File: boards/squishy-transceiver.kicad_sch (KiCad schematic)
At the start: 99 parts, among them Q2 Q_PMOS_DGS, Q3 Q_DUAL_PMOS_S1G1D2S2G2D1, Q4 Q_DUAL_PMOS_S1G1D2S2G2D1, U10 FXL4TD245BQX, U11 FXL4TD245BQX, U12 FXL4TD245BQX, U13 FXL4TD245BQX, U14 FXL4TD245BQX, U15 FXL4TD245BQX, U16 FXL4TD245BQX, U17 THVD1452DGSR, U18 THVD1452DGSR, U19 THVD1452DGSR, U20 THVD1452DGSR, U21 THVD1452DGSR, U22 THVD1452DGSR, U23 THVD1452DGSR, U24 THVD1452DGSR, U25 THVD1452DGSR, U26 THVD1452DGSR, U27 THVD1452DGSR, U28 THVD1452DGSR, U29 THVD1452DGSR, U30 THVD1452DGSR, U31 THVD1452DGSR, U32 THVD1452DGSR, U33 THVD1452DGSR, U34 THVD1452DGSR, U8 FXL4TD245BQX, U9 FXL4TD245BQX

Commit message: hardware: a bunch of clean up and the like
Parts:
- renumbered R51 to R11, R27 to R12, R24 to R15, R57 to R18, R39 to R22, R18 to R23, R48 to R24, R15 to R25, R12 to R26, R45 to R27, R9 to R28, R60 to R29, R33 to R3, R75 to R30, R8 to R31, R76 to R32, R10 to R33, R44 to R34, R78 to R35, R46 to R36, R83 to R37, R73 to R38, R11 to R39, R54 to R4, R77 to R40, R13 to R41, R14 to R42, R16 to R43, R61 to R44, R47 to R45, R84 to R46, R49 to R47, R17 to R48, R19 to R49, R36 to R5, R38 to R50, R40 to R51, R20 to R54, R22 to R55, R23 to R59, R25 to R60, R26 to R61, R28 to R63, R50 to R64, R80 to R65, R52 to R66, R81 to R67, R72 to R68, R29 to R69, R79 to R70, R31 to R71, R62 to R73, R41 to R74, R82 to R75, R43 to R76, R5 to R78, R7 to R79, R42 to R8, R35 to R80, R37 to R81, R53 to R82, R55 to R83, R32 to R84, R34 to R85, R30 to R9, U26 to U1, U29 to U10, U10 to U11, U25 to U13, U32 to U15, U11 to U16, U24 to U17, U23 to U18, U8 to U2, U12 to U20, U34 to U21, U13 to U23, U28 to U24, U21 to U25, U14 to U27, U31 to U28, U20 to U29, U15 to U30, U19 to U31, U30 to U32, U16 to U33, U18 to U34, U33 to U4, U27 to U6, U9 to U8, U17 to U9

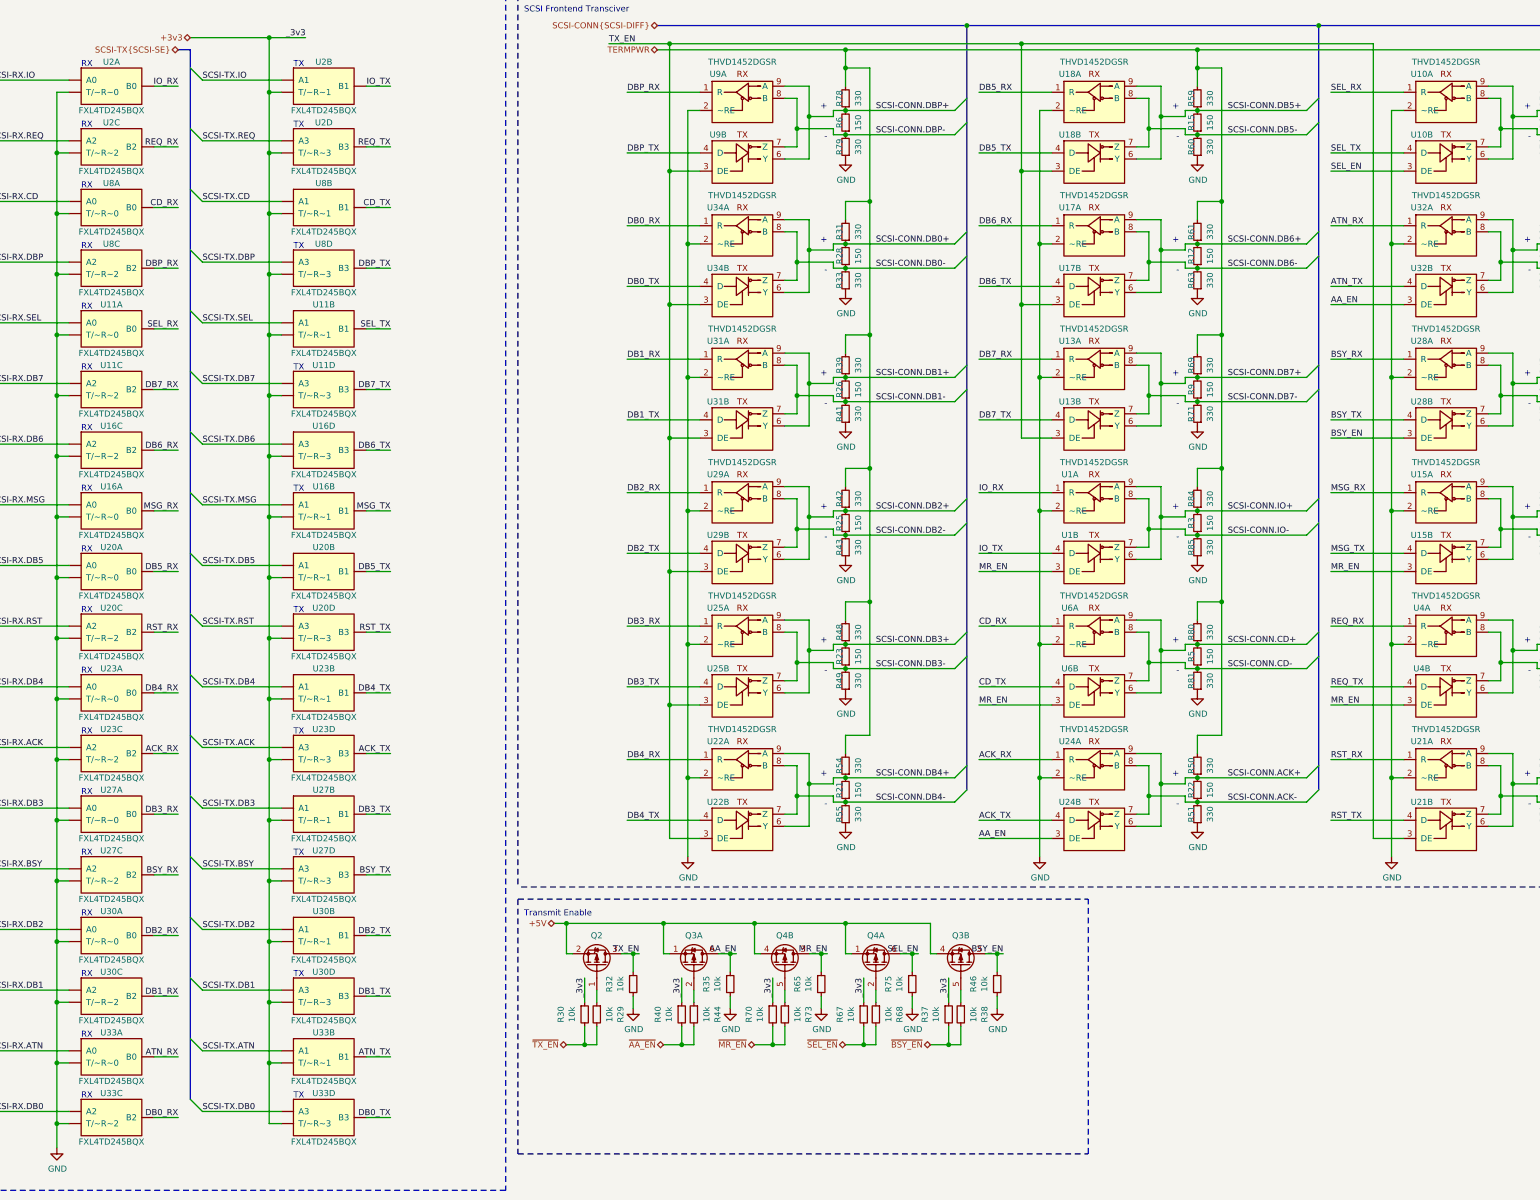
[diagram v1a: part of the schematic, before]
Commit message: hardware: ensured we got a clean bill of health from DRC and ERC
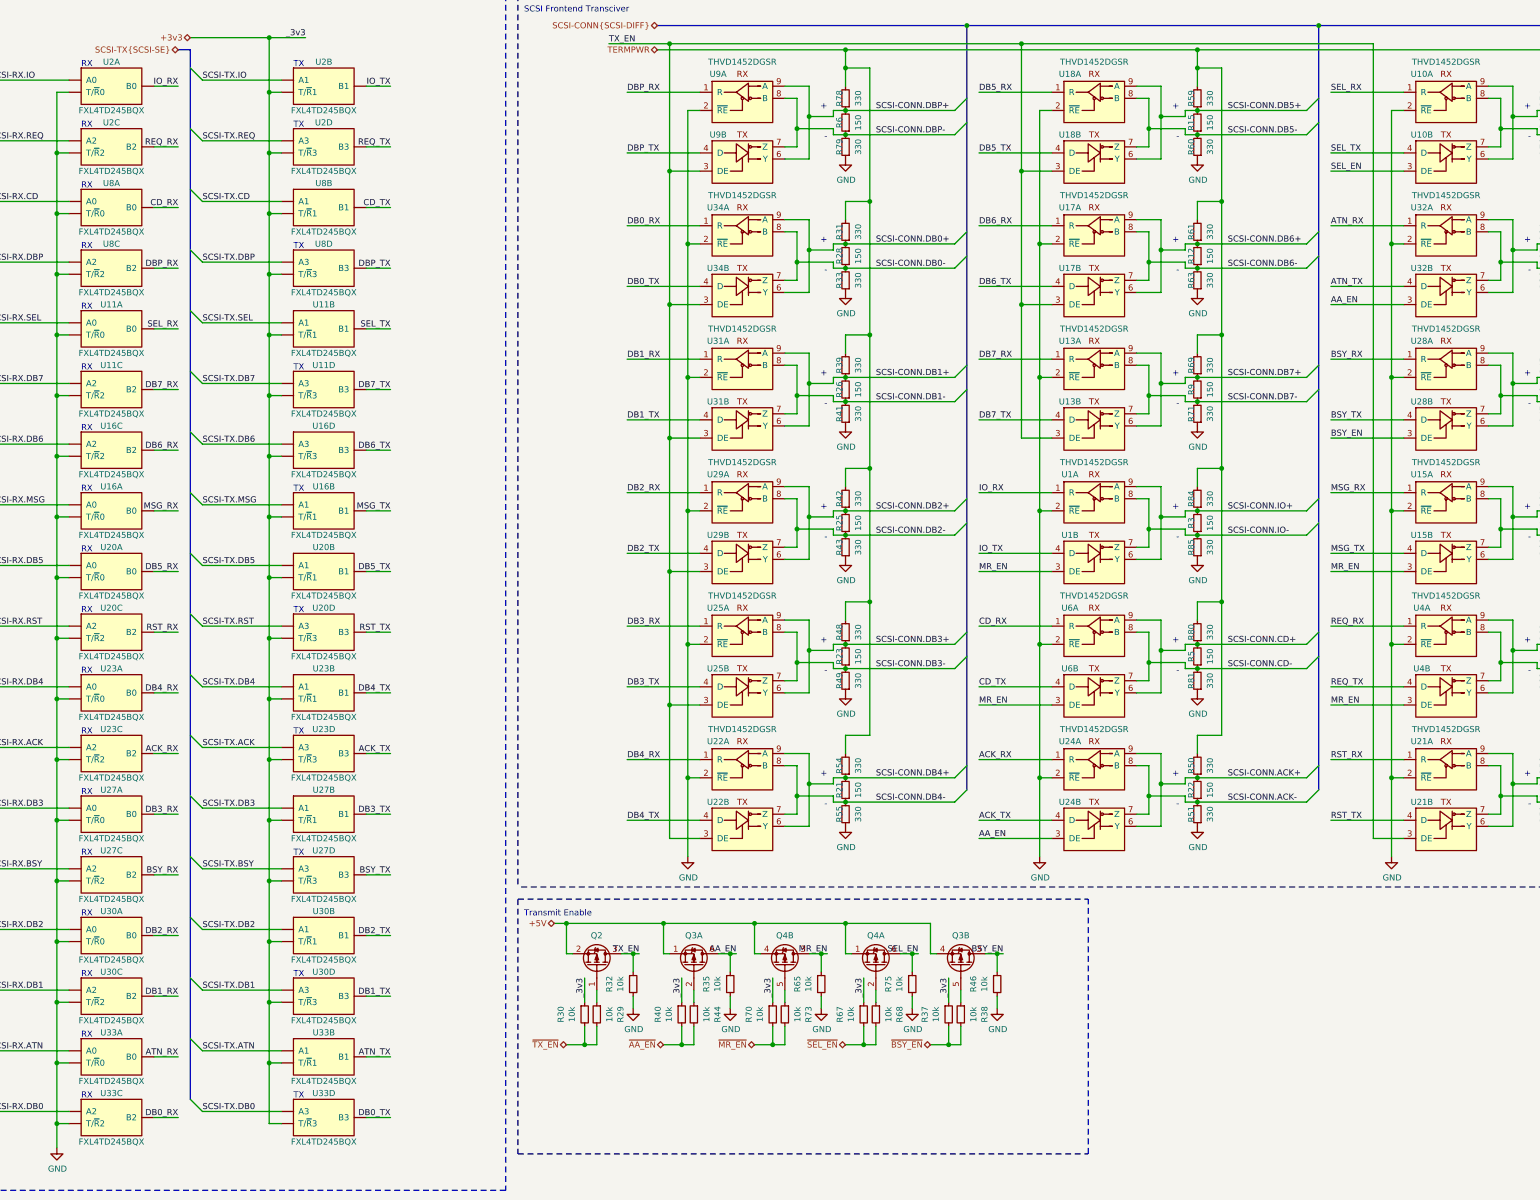
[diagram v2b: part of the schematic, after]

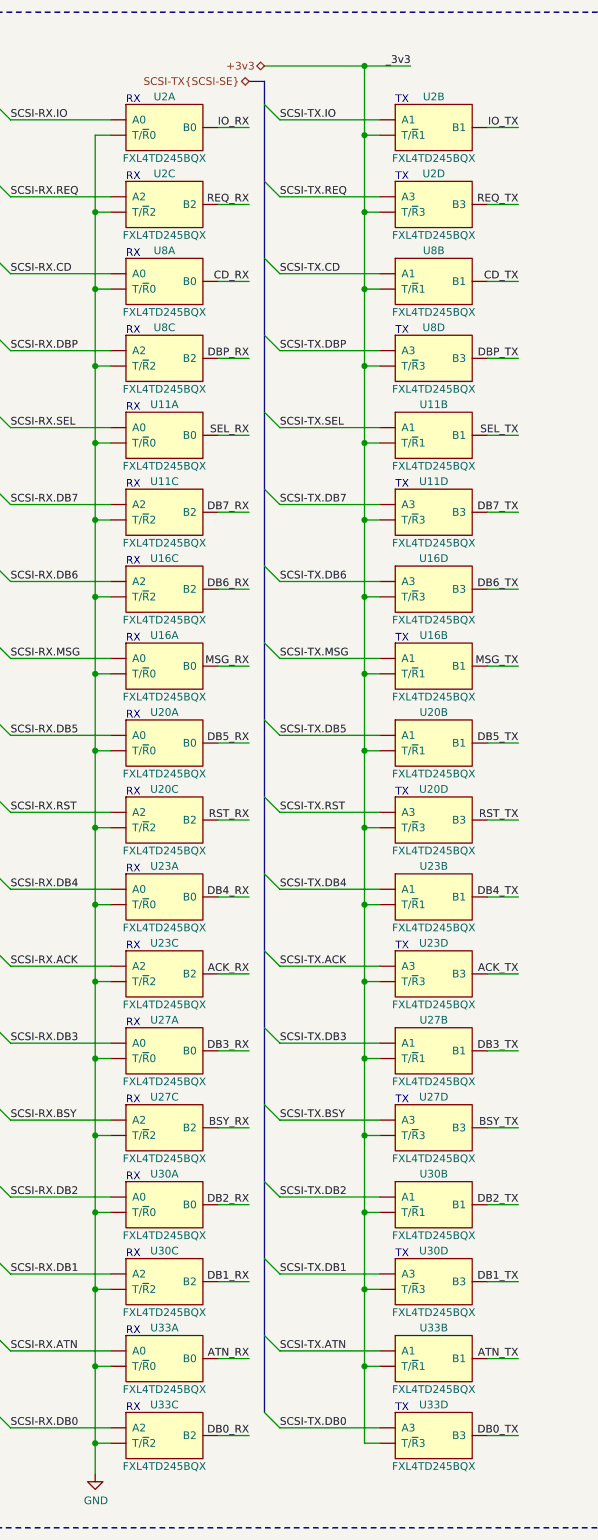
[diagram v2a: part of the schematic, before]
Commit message: hardware: fixed up some datasheets for symbols and added mounting holes
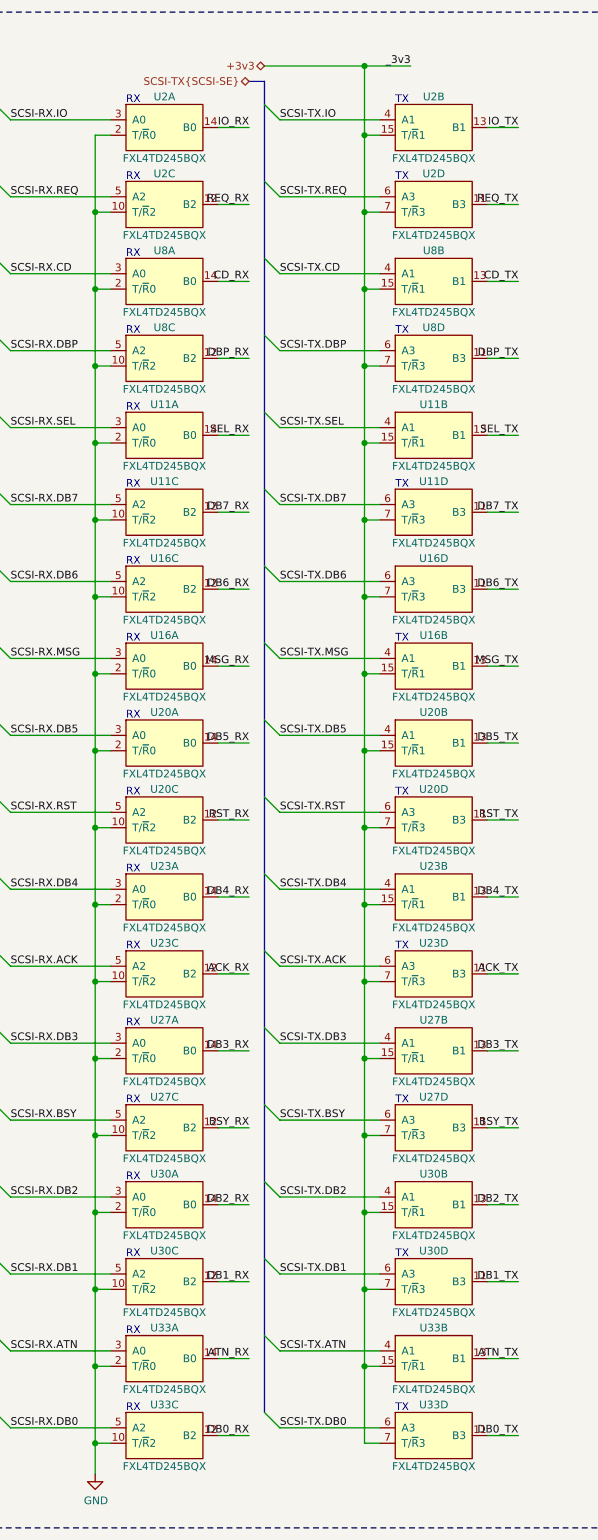
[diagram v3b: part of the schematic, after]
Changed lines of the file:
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@@
       (effects (font (size 1.27 1.27)) hide)
     )
-    (property "Datasheet" "~" (id 3) (at 176.53 217.17 0)
+    (property "Datasheet" "https://www.mouser.com/datasheet/2/427/VISH_S_A0001109972_1-2566876.pdf" (id 3) (at 176.53 217.17 0)
       (effects (font (size 1.27 1.27)) hide)
     )
@@
       (effects (font (size 1.27 1.27)) hide)
     )
-    (property "Datasheet" "~" (id 3) (at 196.85 215.9 0)
+    (property "Datasheet" "https://www.mouser.com/datasheet/2/427/VISHS99213_1-2566626.pdf" (id 3) (at 196.85 215.9 0)
       (effects (font (size 1.27 1.27)) hide)
     )
@@
       (effects (font (size 1.27 1.27)) hide)
     )
-    (property "Datasheet" "~" (id 3) (at 215.9 215.9 0)
+    (property "Datasheet" "https://www.mouser.com/datasheet/2/427/VISHS99213_1-2566626.pdf" (id 3) (at 215.9 215.9 0)
       (effects (font (size 1.27 1.27)) hide)
     )
@@
       (effects (font (size 1.27 1.27)) hide)
     )
-    (property "Datasheet" "~" (id 3) (at 234.95 215.9 0)
+    (property "Datasheet" "https://www.mouser.com/datasheet/2/427/VISHS99213_1-2566626.pdf" (id 3) (at 234.95 215.9 0)
       (effects (font (size 1.27 1.27)) hide)
     )
@@
       (effects (font (size 1.27 1.27)) hide)
     )
-    (property "Datasheet" "~" (id 3) (at 252.73 215.9 0)
+    (property "Datasheet" "https://www.mouser.com/datasheet/2/427/VISHS99213_1-2566626.pdf" (id 3) (at 252.73 215.9 0)
       (effects (font (size 1.27 1.27)) hide)
     )
